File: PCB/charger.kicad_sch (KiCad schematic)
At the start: 13 parts, among them U2 BQ24072RGT

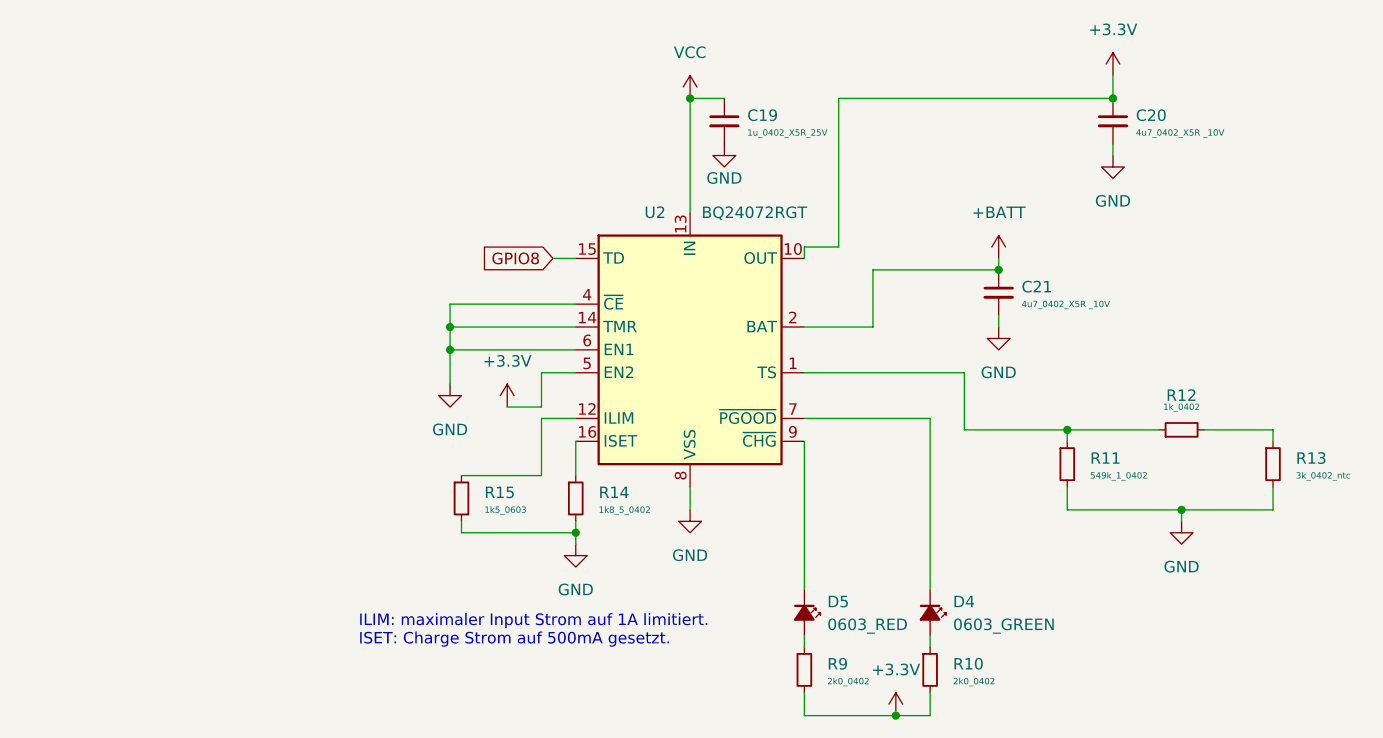
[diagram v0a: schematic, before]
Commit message: Mit dem Layout angefangen
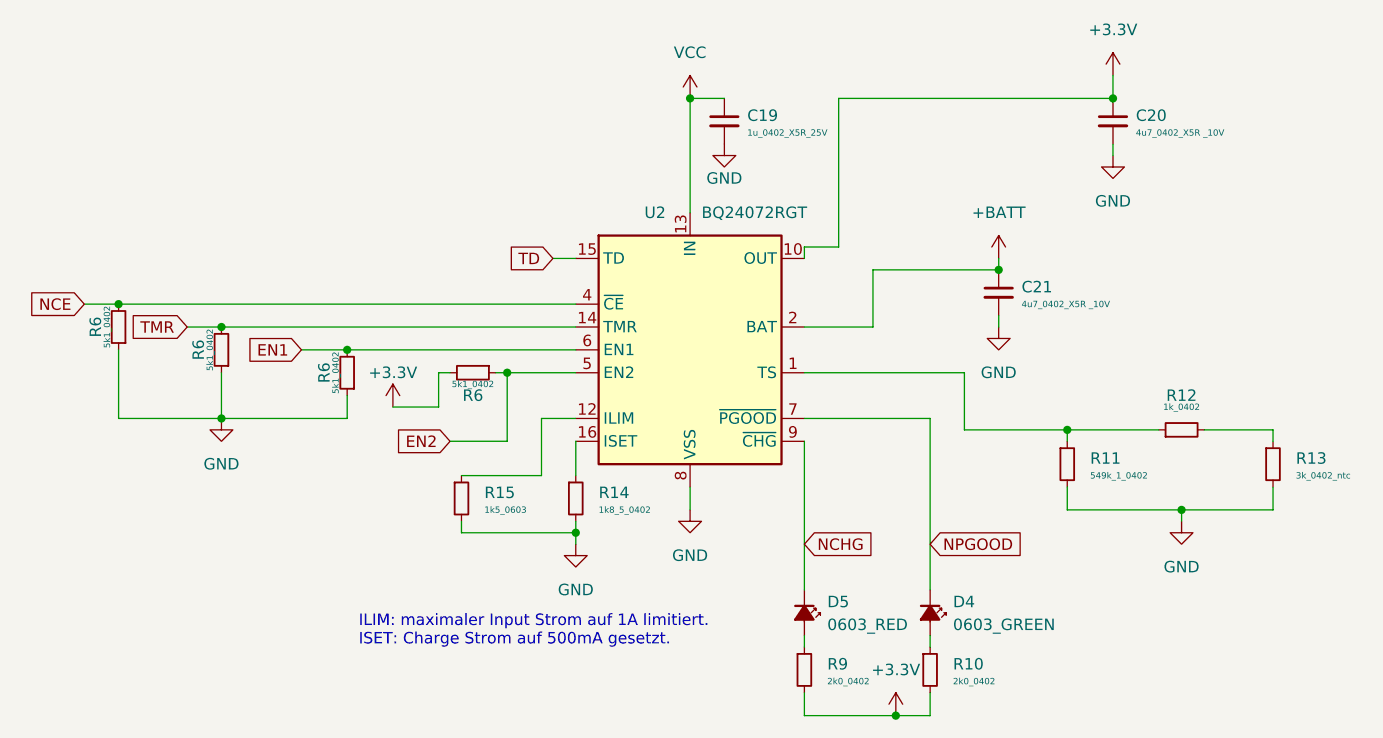
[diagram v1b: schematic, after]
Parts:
- added R6 (x4): 5k1_0402, Resistor_SMD:R_0402_1005Metric, symbol resistor_smd_standard:5k1_0402
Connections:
- net +3.3V: now also R6.2; no longer U2.5 (EN2)
- net GND: now also R6.1, R6.1, R6.1; no longer U2.14 (TMR), U2.4 (~{CE}), U2.6 (EN1)
- net NCHG: now reaches D5.1 (K), U2.9 (~{CHG})
- net NPGOOD: now reaches D4.1 (K), U2.7 (~{PGOOD})
- net GPIO8 renamed TD
- new net EN1: R6.2, U2.6 (EN1)
- new net EN2: R6.1, U2.5 (EN2)
- new net NCE: R6.2, U2.4 (~{CE})
- new net TMR: R6.2, U2.14 (TMR)

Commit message: Layout weiter gemacht.
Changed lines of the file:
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@@
+    )
+  )
+  (netclass_flag "" (length 2.54) (shape round) (at 162.56 72.39 0) (fields_autoplaced)
+    (effects (font (size 1.27 1.27)) (justify left bottom))
+    (property "Netclass" "BAT" (at 163.2585 69.85 0)
+      (effects (font (size 1.27 1.27) italic) (justify left))
+    )
+  )
+  (netclass_flag "" (length 2.54) (shape round) (at 135.89 59.69 90) (fields_autoplaced)
+    (effects (font (size 1.27 1.27)) (justify left bottom))
+    (property "Netclass" "Power" (at 133.35 58.9915 90)
+      (effects (font (size 1.27 1.27) italic) (justify left))
+    )
+  )
+  (netclass_flag "" (length 2.54) (shape round) (at 163.83 53.34 0) (fields_autoplaced)
+    (effects (font (size 1.27 1.27)) (justify left bottom))
+    (property "Netclass" "3V3" (at 164.5285 50.8 0)
+      (effects (font (size 1.27 1.27) italic) (justify left))
     )
   )
@@
       (effects (font (size 1.27 1.27)) hide)
     )
-    (property "Value" "+3.3V" (at 102.87 83.82 0)
+    (property "Value" "+3.3V" (at 102.87 84.074 0)
       (effects (font (size 1.27 1.27)))
     )
@@
       (effects (font (size 1.27 1.27)))
     )
-    (property "Value" "5k1_0402" (at 82.55 81.28 90)
-      (effects (font (size 0.7 0.7)))
+    (property "Value" "5k1_0402" (at 82.55 81.28 0)
+      (effects (font (size 0.7 0.7)) (justify left))
     )
     (property "Footprint" "Resistor_SMD:R_0402_1005Metric" (at 100.33 69.85 0)
@@
       (effects (font (size 1.27 1.27)))
     )
-    (property "Value" "5k1_0402" (at 111.76 85.09 90)
-      (effects (font (size 0.7 0.7)))
+    (property "Value" "5k1_0402" (at 111.76 85.09 0)
+      (effects (font (size 0.7 0.7)) (justify left))
     )
     (property "Footprint" "Resistor_SMD:R_0402_1005Metric" (at 100.33 67.31 0)
@@
       (effects (font (size 1.27 1.27)))
     )
-    (property "Value" "5k1_0402" (at 71.12 78.74 90)
-      (effects (font (size 0.7 0.7)))
+    (property "Value" "5k1_0402" (at 71.12 78.74 0)
+      (effects (font (size 0.7 0.7)) (justify left))
     )
     (property "Footprint" "Resistor_SMD:R_0402_1005Metric" (at 88.9 67.31 0)
@@
       (effects (font (size 1.27 1.27)))
     )
-    (property "Value" "5k1_0402" (at 96.52 83.82 90)
-      (effects (font (size 0.7 0.7)))
+    (property "Value" "5k1_0402" (at 96.52 83.82 0)
+      (effects (font (size 0.7 0.7)) (justify left))
     )
     (property "Footprint" "Resistor_SMD:R_0402_1005Metric" (at 114.3 72.39 0)
@@
       (effects (font (size 1.27 1.27)) (justify left))
     )
-    (property "Value" "BQ24072RGT" (at 137.16 66.04 0)
-      (effects (font (size 1.27 1.27)) (justify left))
+    (property "Value" "BQ24072RGT" (at 152.4 67.31 0)
+      (effects (font (size 1.27 1.27)) (justify right))
     )
     (property "Footprint" "Package_DFN_QFN:VQFN-16-1EP_3x3mm_P0.5mm_EP1.6x1.6mm" (at 143.51 95.25 0)

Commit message: update
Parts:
- U2: LCSC (none) -> C140288
- renumbered R6 to R16, R6 to R17, R6 to R4, R6 to R5

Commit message: updated
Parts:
- removed R14: 1k8_5_0402, Resistor_SMD:R_0402_1005Metric, symbol resistor_smd_extended:1k8_5_0402
- added R18: 8k2_0402, Resistor_SMD:R_0402_1005Metric, symbol resistor_smd_standard:8k2_0402
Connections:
- net GND: now also R18.2
- net at U2.16 (ISET): now also R18.1
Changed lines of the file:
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@@
-	)
-	(symbol
-		(lib_id "resistor_smd_extended:1k8_5_0402")
-		(at 123.19 97.79 0)
-		(unit 1)
-		(exclude_from_sim no)
-		(in_bom yes)
-		(on_board yes)
-		(dnp no)
-		(fields_autoplaced yes)
-		(property "Reference" "R14"
-			(at 125.73 97.155 0)
-			(effects
-				(font
-					(size 1.27 1.27)
-				)
-				(justify left)
-			)
-		)
-		(property "Value" "1k8_5_0402"
-			(at 125.73 99.06 0)
-			(effects
-				(font
-					(size 0.7 0.7)
-				)
-				(justify left)
-			)
-		)
-		(property "Footprint" "Resistor_SMD:R_0402_1005Metric"
-			(at 123.825 100.965 0)
-			(effects
-				(font
-					(size 1.27 1.27)
-				)
-				(hide yes)
-			)
-		)
-		(property "Datasheet" "https://datasheet.lcsc.com/lcsc/2206010045_UNI-ROYAL-Uniroyal-Elec-0402WGJ0182TCE_C25932.pdf"
-			(at 123.19 100.965 0)
-			(effects
-				(font
-					(size 1.27 1.27)
-				)
-				(hide yes)
-			)
-		)
-		(property "Description" ""
-			(at 123.19 97.79 0)
-			(effects
-				(font
-					(size 1.27 1.27)
-				)
-				(hide yes)
-			)
-		)
-		(property "LCSC" "C25932"
-			(at 123.825 100.965 0)
-			(effects
-				(font
-					(size 1.27 1.27)
-				)
-				(hide yes)
-			)
-		)
-		(property "Tollerance" "5%"
-			(at 125.095 99.06 0)
-			(effects
-				(font
-					(size 0.7 0.7)
-				)
-				(hide yes)
-			)
-		)
-		(pin "1"
-		)
-		(pin "2"
-		)
-		(instances
-			(project "ESP32-C3"
-				(path "/35961fef-fe97-49ba-90a9-cbb988ec3bed/fa53471f-70aa-4ce3-99ec-d97d3fb2988c"
-					(reference "R14")
-					(unit 1)
-				)
-			)
-		)
 	)
 	(symbol
@@
 					(unit 1)
 				)
+			)
+		)
+	)
+	(symbol
+		(lib_id "resistor_smd_standard:8k2_0402")
+		(at 123.19 97.79 0)
+		(unit 1)
+		(exclude_from_sim no)
+		(in_bom yes)
+		(on_board yes)
+		(dnp no)
+		(fields_autoplaced yes)
+		(property "Reference" "R18"
+			(at 125.73 97.1549 0)
+			(effects
+				(font
+					(size 1.27 1.27)
+				)
+				(justify left)
+			)
+		)
+		(property "Value" "8k2_0402"
+			(at 125.73 99.06 0)
+			(effects
+				(font
+					(size 0.7 0.7)
+				)
+				(justify left)
+			)
+		)
+		(property "Footprint" "Resistor_SMD:R_0402_1005Metric"
+			(at 123.825 100.965 0)
+			(effects
+				(font
+					(size 1.27 1.27)
+				)
+				(hide yes)
+			)
+		)
+		(property "Datasheet" "https://datasheet.lcsc.com/lcsc/2206010045_UNI-ROYAL-Uniroyal-Elec-0402WGF8201TCE_C25924.pdf"
+			(at 123.19 100.965 0)
+			(effects
+				(font
+					(size 1.27 1.27)
+				)
+				(hide yes)
+			)
+		)
+		(property "Description" "62.5mW Thick Film Resistors ±100ppm/℃ ±1% 8.2kΩ 0402  Chip Resistor - Surface Mount ROHS"
+			(at 123.19 97.79 0)
+			(effects
+				(font
+					(size 1.27 1.27)
+				)
+				(hide yes)
+			)
+		)
+		(property "LCSC" "C25924"
+			(at 123.825 100.965 0)
+			(effects
+				(font
+					(size 1.27 1.27)
+				)
+				(hide yes)
+			)
+		)
+		(property "PriceReel" "0.0003"
+			(at 123.19 97.79 0)
+			(effects
+				(font
+					(size 1.27 1.27)
+				)
+				(hide yes)
+			)
+		)
+		(property "QtyReel" "10000"
+			(at 123.19 97.79 0)
+			(effects
+				(font
+					(size 1.27 1.27)
+				)
+				(hide yes)
+			)
+		)
+		(pin "1"
+		)
+		(pin "2"
+		)
+		(instances
+			(project "ESP32-C3"
+				(path "/35961fef-fe97-49ba-90a9-cbb988ec3bed/fa53471f-70aa-4ce3-99ec-d97d3fb2988c"
+					(reference "R18")
+					(unit 1)
+				)

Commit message: Zur Kontrolle fertig.
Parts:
- C20, C21: LCSC C5252390 -> C2932473
- D4: LCSC C72043 -> C5179616
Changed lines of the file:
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@@
 			)
 		)
-		(property "LCSC" "C5252390"
+		(property "LCSC" "C2932473"
 			(at 170.18 74.93 0)
 			(effects
@@
 			)
 		)
-		(property "LCSC" "C72043"
+		(property "LCSC" "C5179616"
 			(at 162.56 110.49 0)
 			(effects
@@
 			)
 		)
-		(property "LCSC" "C5252390"
+		(property "LCSC" "C2932473"
 			(at 182.88 55.88 0)
 			(effects

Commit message: Neuste Version
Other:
- note added: "ILIM: maximaler Input Strom auf 1A limitiert. ISET: Charge Strom auf ~100mA gesetzt."
- note removed: "ILIM: maximaler Input Strom auf 1A limitiert. ISET: Charge Strom auf 500mA gesetzt."
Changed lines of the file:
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@@
 		)
 	)
-	(text "ILIM: maximaler Input Strom auf 1A limitiert.\nISET: Charge Strom auf 500mA gesetzt."
+	(text "ILIM: maximaler Input Strom auf 1A limitiert.\nISET: Charge Strom auf ~100mA gesetzt."
 		(exclude_from_sim no)
 		(at 99.06 114.3 0)

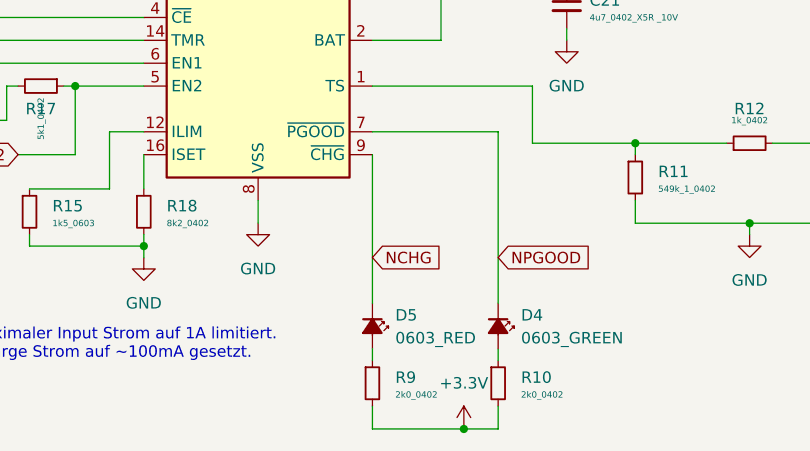
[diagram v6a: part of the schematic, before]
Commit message: Boot Button hinzugefügt
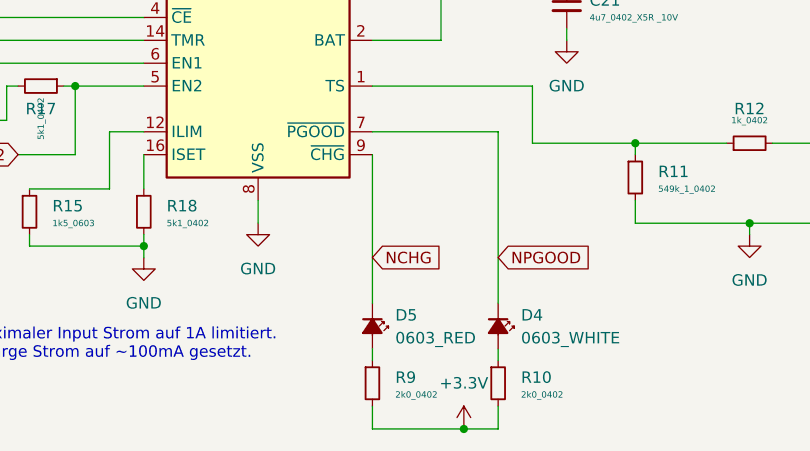
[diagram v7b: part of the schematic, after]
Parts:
- C20, C21: LCSC C2932473 -> C23733
- D4: value 0603_GREEN -> 0603_WHITE; LCSC C5179616 -> C2290
- R18: value 8k2_0402 -> 5k1_0402; LCSC C25924 -> C25905
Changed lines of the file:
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@@
 			)
 		)
-		(property "LCSC" "C2932473"
+		(property "LCSC" "C23733"
 			(at 170.18 74.93 0)
 			(effects
@@
 			)
 		)
-		(property "Value" "0603_GREEN"
+		(property "Value" "0603_WHITE"
 			(at 165.1 111.8235 90)
 			(effects
@@
 			)
 		)
-		(property "Datasheet" "https://datasheet.lcsc.com/lcsc/1811101510_Everlight-Elec-19-217-GHC-YR1S2-3T_C72043.pdf"
+		(property "Datasheet" "https://wmsc.lcsc.com/wmsc/upload/file/pdf/v2/lcsc/2305091500_Hubei-KENTO-Elec-KT-0603W_C2290.pdf"
 			(at 162.56 110.49 90)
 			(effects
@@
 			)
 		)
-		(property "LCSC" "C5179616"
+		(property "LCSC" "C2290"
 			(at 162.56 110.49 0)
 			(effects
@@
 			)
 		)
-		(property "LCSC" "C2932473"
+		(property "LCSC" "C23733"
 			(at 182.88 55.88 0)
 			(effects
@@
 			)
 		)
-		(property "Value" "8k2_0402"
+		(property "Value" "5k1_0402"
 			(at 125.73 99.06 0)
 			(effects
@@
 			)
 		)
-		(property "Description" "62.5mW Thick Film Resistors ±100ppm/℃ ±1% 8.2kΩ 0402  Chip Resistor - Surface Mount ROHS"
+		(property "Description" "62.5mW Thick Film Resistors 50V ±100ppm/℃ ±1% 5.1kΩ 0402 Chip Resistor - Surface Mount ROHS"
 			(at 123.19 97.79 0)
 			(effects
@@
 			)
 		)
-		(property "LCSC" "C25924"
+		(property "LCSC" "C25905"
 			(at 123.825 100.965 0)
 			(effects

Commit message: Wichtige Änderungen für die Fertigung
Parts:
- removed R11: 549k_1_0402, Resistor_SMD:R_0402_1005Metric, symbol resistor_smd_extended:549k_1_0402
- removed R12: 1k_0402, Resistor_SMD:R_0402_1005Metric, symbol resistor_smd_standard:1k_0402
- removed R13: 3k_0402_ntc, Resistor_SMD:R_0402_1005Metric, symbol 2_ntc:3k_0402_ntc
- added R11: 10k_0402, Resistor_SMD:R_0402_1005Metric, symbol resistor_smd_standard:10k_0402
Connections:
- net GND: now also R11.2
- net at U2.1 (TS): now also R11.1
